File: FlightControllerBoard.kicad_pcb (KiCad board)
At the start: 2 copper layers, 60 x 40 mm, 82 parts, among them J1 Conn_01x02, J10 Conn_01x02, J11 Conn_01x02, J12 Conn_01x03_Male, J13 USB_C_Receptacle_USB2.0, J14 Conn_02x03_Odd_Even, J2 Conn_01x03_Male, J3 Conn_01x03_Male, J4 Conn_01x03_Male, J5 Conn_01x03_Male, J6 Conn_01x03_Male, J7 Conn_01x03_Male, J8 Conn_01x03_Male, J9 Conn_01x03_Male, Q1 BSS138, SW1 SW_Push, SW2 SW_Push, U1 FT230XQ, U2 LMZM23600, U3 ATmega2560-16AU, U4 BNO055, Y1 16MHz, Y2 32.768kHz

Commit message: use submodule for FT230
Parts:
- removed the R8 at (59.0, 71.5)
- removed the R9 at (59.0, 73.5)
- added C5: 4.7µF, Capacitor_SMD:C_0603_1608Metric, F.Cu at (5.52, 0.76)
- moved C4 43.8 mm to (1.51, 0.76), turned to 0 degrees
- renumbered C9 to C10, C10 to C11, C11 to C12, C12 to C13, C13 to C14, C14 to C15, C15 to C16, C16 to C17, C17 to C18, C18 to C19, C19 to C20, C20 to C21, C5 to C6, C6 to C7, C7 to C8, C8 to C9, R12 to R10, R13 to R11, R14 to R12, R15 to R13, R16 to R14, R17 to R15, R18 to R16, R19 to R17, R20 to R18, R21 to R19, R22 to R20, R23 to R21, R24 to R22, R25 to R23, R26 to R24, R10 to R8, R11 to R9
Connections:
- C4 pad 1: VBUS -> /FT230/5VOUT

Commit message: pullups, jumpers
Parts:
- removed the J10 at (258.0, 77.0)
- removed the J11 at (254.0, 77.0)
- added JP1: Jumper_NO_Small, Connector_PinHeader_2.54mm:PinHeader_1x02_P2.54mm_Vertical, F.Cu at (127.8, -48.2)
- added JP2: Jumper_NO_Small, Connector_PinHeader_2.54mm:PinHeader_1x02_P2.54mm_Vertical, F.Cu at (132.5, -48.2)
- added R1: 4.7k, Resistor_SMD:R_0603_1608Metric, F.Cu at (136.8, -49.2)
- added R2: 4.7k, Resistor_SMD:R_0603_1608Metric, F.Cu at (136.8, -46.7)
- renumbered J12 to J10, J13 to J11, J14 to J12, R8 to R10, R9 to R11, R10 to R12, R11 to R13, R12 to R14, R13 to R15, R14 to R16, R15 to R17, R16 to R18, R17 to R19, R18 to R20, R19 to R21, R20 to R22, R21 to R23, R22 to R24, R23 to R25, R24 to R26, R1 to R3, R2 to R4, R3 to R5, R4 to R6, R5 to R7, R6 to R8, R7 to R9

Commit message: layout
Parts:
- removed SW2: SW_Push, Button_Switch_SMD:SW_SPST_PTS810
- added H1: MountingHole, MountingHole:MountingHole_3.2mm_M3, F.Cu at (45.0, 55.0)
- added H2: MountingHole, MountingHole:MountingHole_3.2mm_M3, F.Cu at (5.00, 20.0)
- added H3: MountingHole, MountingHole:MountingHole_3.2mm_M3, F.Cu at (45.0, 20.0)
- added H4: MountingHole, MountingHole:MountingHole_3.2mm_M3, F.Cu at (5.00, 55.0)
- added REF**: ToolboxLogo, Toolbox:ToolboxLogo, F.Cu at (8.25, 47.0)
- J1: footprint XT30:XT30PB-M -> Connector_AMASS:AMASS_XT30UPB-M_1x02_P5.0mm_Vertical
- moved D2 239.7 mm to (18.8, 55.8), turned to 90 degrees
- moved R5 239.3 mm to (18.8, 52.5), turned to 270 degrees
- moved SW1 237.9 mm to (3.25, 13.5), turned to 180 degrees
- moved D1 227.7 mm to (17.0, 55.8), turned to 90 degrees
- moved R4 227.3 mm to (17.0, 52.5), turned to 270 degrees
- moved C19 224.6 mm to (15.5, 39.0), turned to 180 degrees
- moved Y2 221.4 mm to (15.5, 42.0), turned to 90 degrees
- moved C20 219.4 mm to (14.5, 45.8), turned to 270 degrees
- moved U4 218.7 mm to (19.5, 41.0), turned to 90 degrees
- moved C18 215.9 mm to (16.2, 45.8), turned to 270 degrees
- moved R26 213.3 mm to (18.8, 46.8), turned to 180 degrees
- moved C16 211.9 mm to (22.0, 45.0), turned to 0 degrees
- moved C21 211.7 mm to (18.8, 45.0), turned to 180 degrees
- moved R1 135.6 mm to (33.0, 38.0), turned to 180 degrees
- moved R2 132.9 mm to (33.0, 36.2), turned to 180 degrees
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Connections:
- U3 pad 35: (no net) -> Net-(R15-Pad1)
- U3 pad 36: (no net) -> Net-(R16-Pad1)
- U3 pad 37: (no net) -> Net-(R17-Pad1)
- U3 pad 38: (no net) -> Net-(R18-Pad1)
- U3 pad 39: (no net) -> Net-(R19-Pad1)
- U3 pad 40: (no net) -> Net-(R20-Pad1)
- U3 pad 41: (no net) -> Net-(R21-Pad1)
- U3 pad 42: (no net) -> Net-(R22-Pad1)
- U3 pad 53: Net-(R15-Pad1) -> (no net)
- U3 pad 54: Net-(R16-Pad1) -> (no net)
- U3 pad 55: Net-(R17-Pad1) -> (no net)
- U3 pad 56: Net-(R18-Pad1) -> (no net)
- U3 pad 57: Net-(R19-Pad1) -> (no net)
- U3 pad 58: Net-(R20-Pad1) -> (no net)
- U3 pad 59: Net-(R21-Pad1) -> (no net)
- U3 pad 60: Net-(R22-Pad1) -> (no net)
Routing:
- net +3V3: track 24.9 -> 161.8 mm, vias 0 -> 6
- net /ATMega/~RESET~: track 0.00 -> 52.4 mm, vias 0 -> 2
- net +5V: track 74.0 -> 119.0 mm, vias 0 -> 2
- net /FT230/RX: track 1.07 -> 30.5 mm, vias 0 -> 2
- net /ATMega/RX0: track 0.00 -> 25.8 mm, vias 0 -> 2
- net GNDS: track 0.00 -> 16.8 mm, vias 0 -> 2
- net /ATMega/RX1: track 0.00 -> 14.8 mm
- net Net-(R22-Pad1): track 4.96 -> 19.6 mm, vias 0 -> 2
- net Net-(R21-Pad1): track 4.76 -> 18.5 mm, vias 0 -> 2
- net /BNO/INT: track 0.00 -> 13.5 mm, vias 0 -> 2
- net /BNO/RX: track 0.00 -> 12.6 mm
- net Net-(R20-Pad1): track 5.38 -> 17.4 mm, vias 0 -> 2
- net /FT230/5VOUT: track 5.12 -> 17.1 mm, vias 0 -> 1
- net /ATMega/MOSI: track 16.6 -> 28.4 mm
- net /ATMega/SCK: track 15.5 -> 26.5 mm
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- added copper zone on F.Cu, net GNDS
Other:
- board size 60 x 40 mm -> 50 x 60 mm
- net class Default: clearance 0.2 -> 0.15; trace_width 0.25 -> 0.2; via_dia 0.8 -> 0.5; via_drill 0.4 -> 0.25
- rule trace_clearance: 0.2 -> 0.15
- board text added: "1"
- board text added: "2"
- board text added: "3"
- board text added: "3V"
- board text added: "4"
- board text added: "5"
- board text added: "5V"
- board text added: "5V In"
- board text added: "6"
- board text added: "7"
- board text added: "8"
- board text added: "GND"
- board text added: "ICSP"
- board text added: "REMOVE BEFORE FLIGHT"
- board text added: "RX"
- board text added: "SB"
- board text added: "TX"

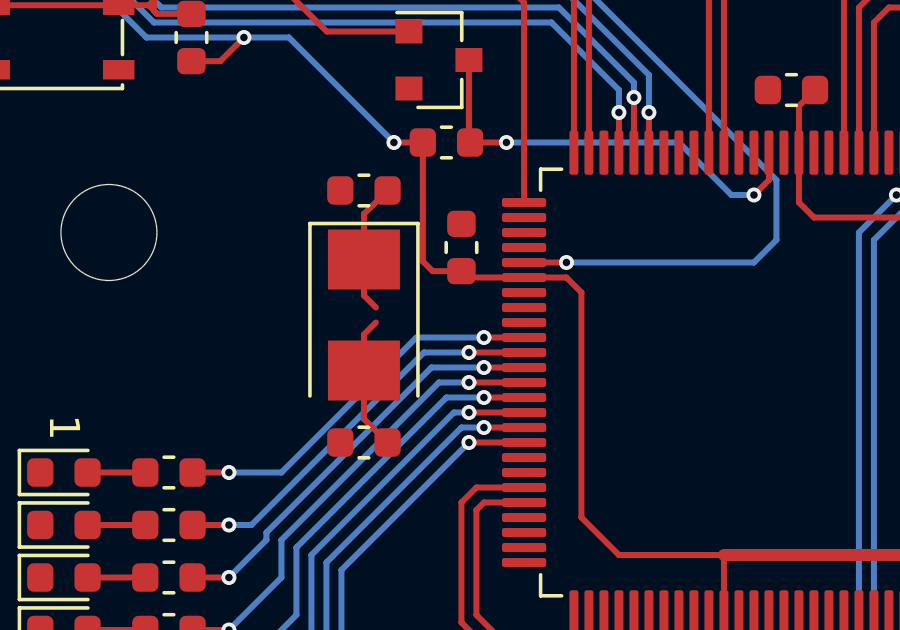
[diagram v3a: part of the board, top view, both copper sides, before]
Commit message: fix Y1 connection
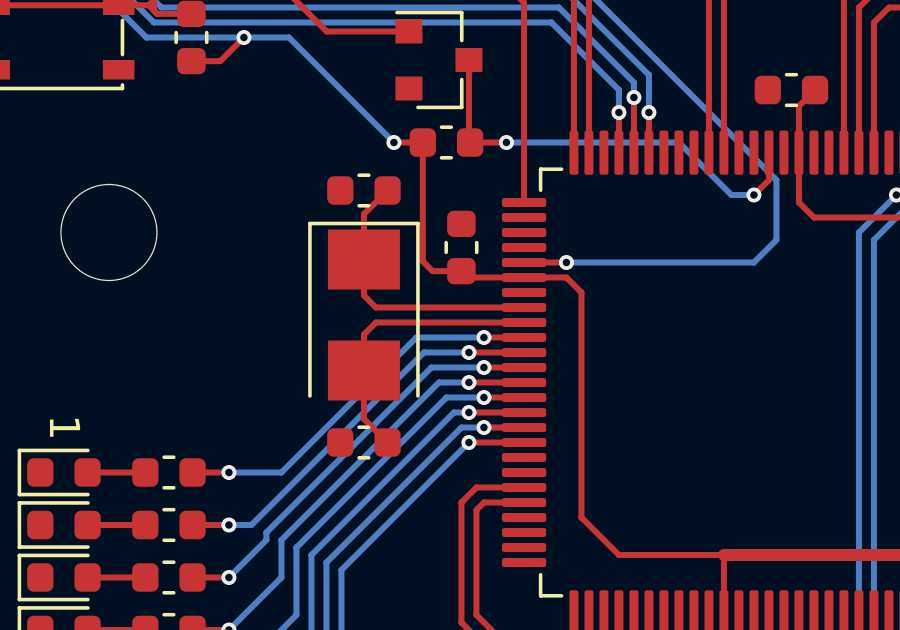
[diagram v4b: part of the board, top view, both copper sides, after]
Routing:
- net Net-(C9-Pad1): track 4.49 -> 9.43 mm
- net Net-(C10-Pad1): track 4.39 -> 9.33 mm
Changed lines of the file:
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@@
     (thickness 1.6)
     (drawings 35)
-    (tracks 485)
+    (tracks 487)
     (zones 0)
     (modules 87)
@@
   (segment (start 13.5 23.4) (end 13.5 24.6) (width 0.2) (layer F.Cu) (net 44) (status 20))
   (segment (start 13.9 23) (end 13.5 23.4) (width 0.2) (layer F.Cu) (net 44))
+  (segment (start 13.9 23) (end 18.8375 23) (width 0.2) (layer F.Cu) (net 44))
   (segment (start 15.5 39.7875) (end 16.2875 39) (width 0.2) (layer F.Cu) (net 45) (status 20))
   (segment (start 15.5 40.75) (end 15.5 39.7875) (width 0.2) (layer F.Cu) (net 45) (status 10))
@@
   (segment (start 13.5 22.1) (end 13.5 20.9) (width 0.2) (layer F.Cu) (net 51) (status 20))
   (segment (start 13.9 22.5) (end 13.5 22.1) (width 0.2) (layer F.Cu) (net 51))
+  (segment (start 13.9 22.5) (end 18.8375 22.5) (width 0.2) (layer F.Cu) (net 51))
   (segment (start 22.7125 41.75) (end 22.75 41.7125) (width 0.2) (layer F.Cu) (net 52) (status 30))
   (segment (start 21.1625 41.75) (end 22.7125 41.75) (width 0.2) (layer F.Cu) (net 52) (status 30))

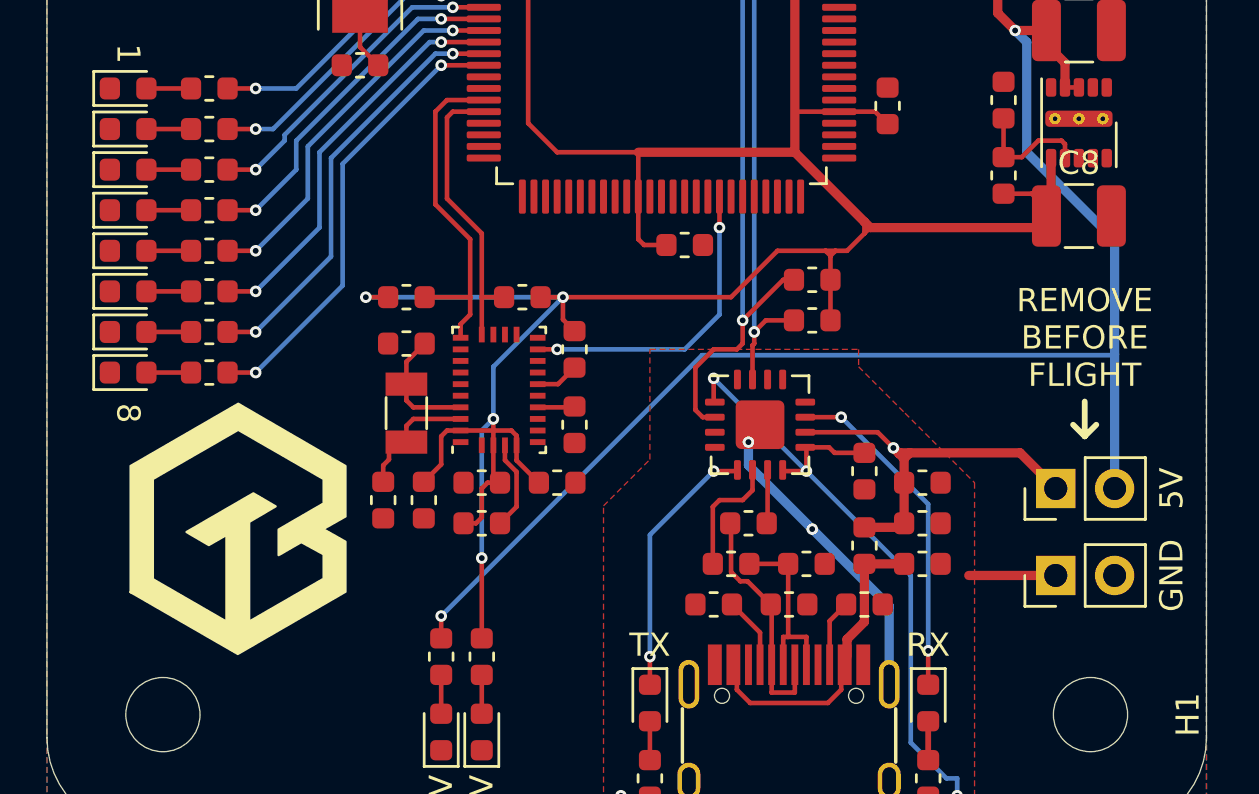
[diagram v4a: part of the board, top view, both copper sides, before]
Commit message: small layout fixes
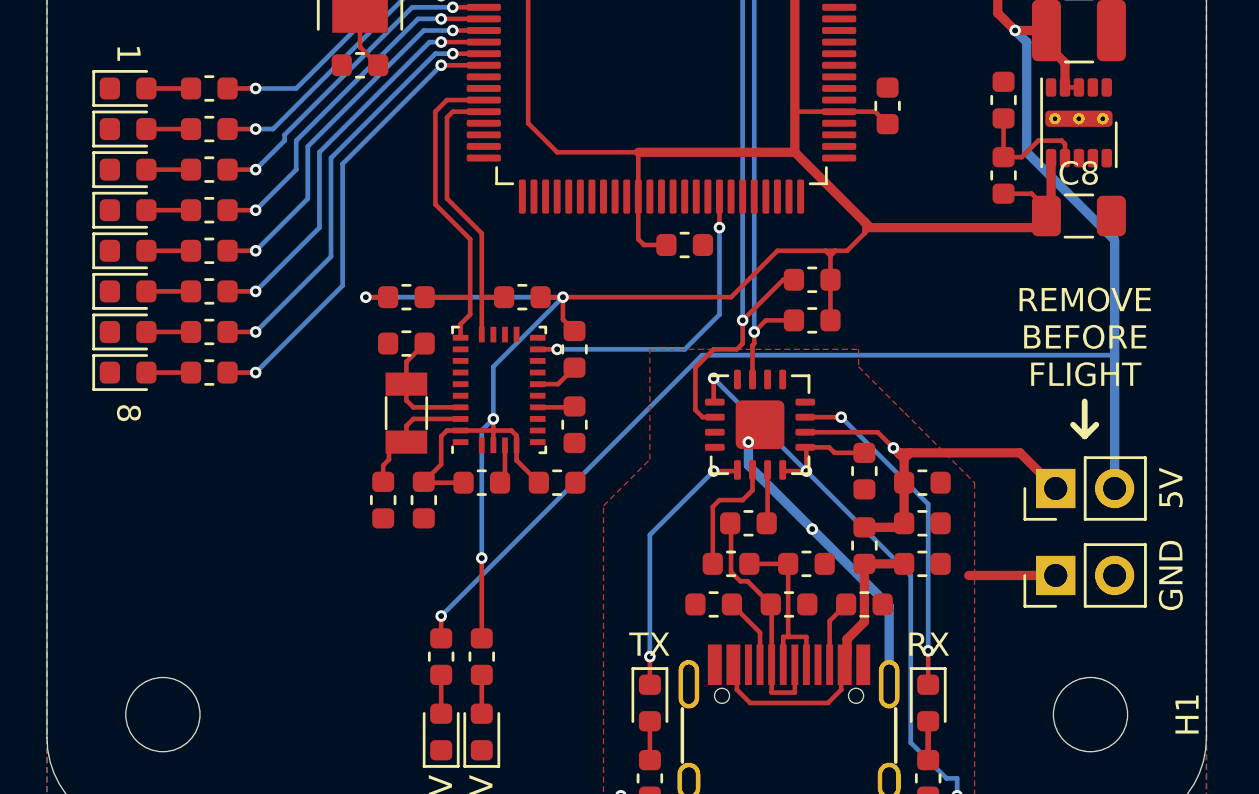
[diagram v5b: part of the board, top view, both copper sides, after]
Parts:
- removed C21: 6.8nF, Capacitor_SMD:C_0603_1608Metric
- removed REF**: ToolboxLogo, Toolbox:ToolboxLogo
- C18: value 120nF -> 100nF
- C19, C20: value 12.5pF -> 9pF
- C8: value 33µF -> 22µF; footprint Capacitor_SMD:C_1210_3225Metric -> Capacitor_SMD:C_1206_3216Metric
- moved R26 1.75 mm to (18.8, 45.0)
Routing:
- net +3V3: track 161.8 -> 158.8 mm
- net Net-(R26-Pad1): track 3.86 -> 1.70 mm

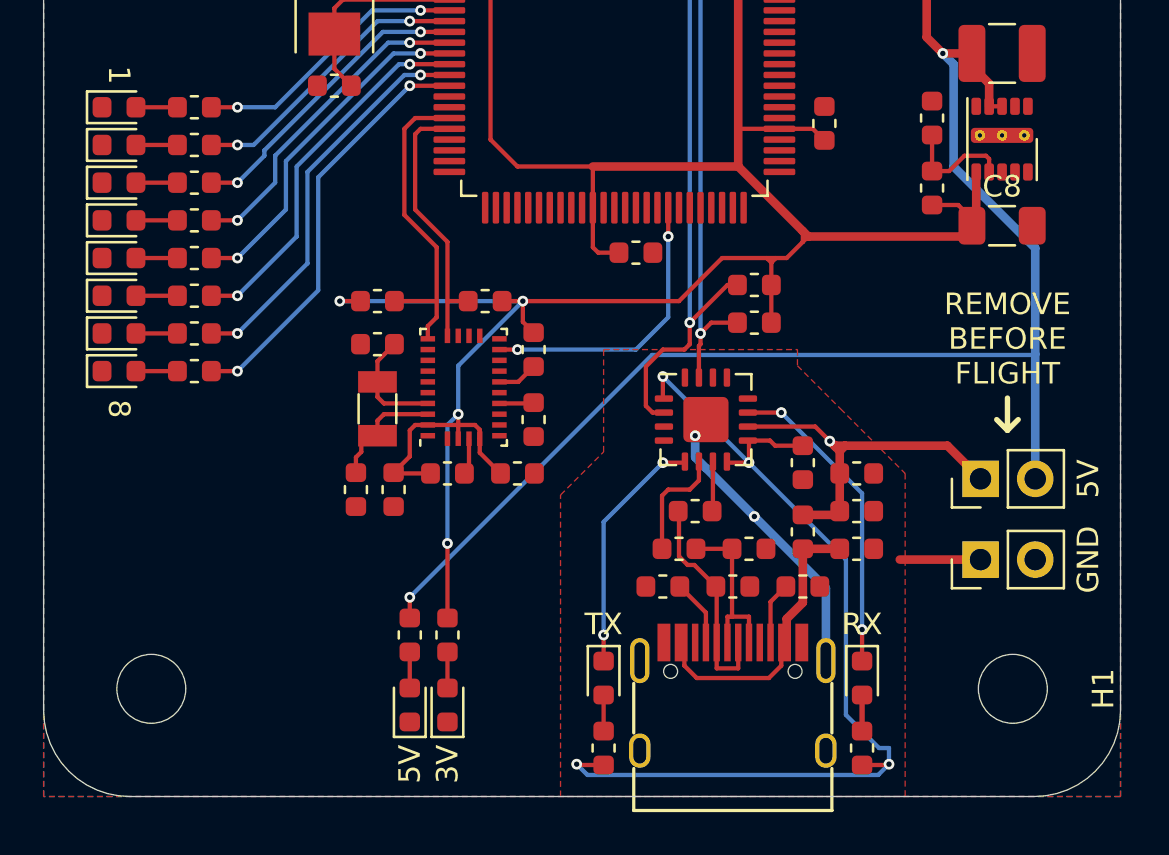
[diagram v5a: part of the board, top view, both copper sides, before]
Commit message: silkscreen logos
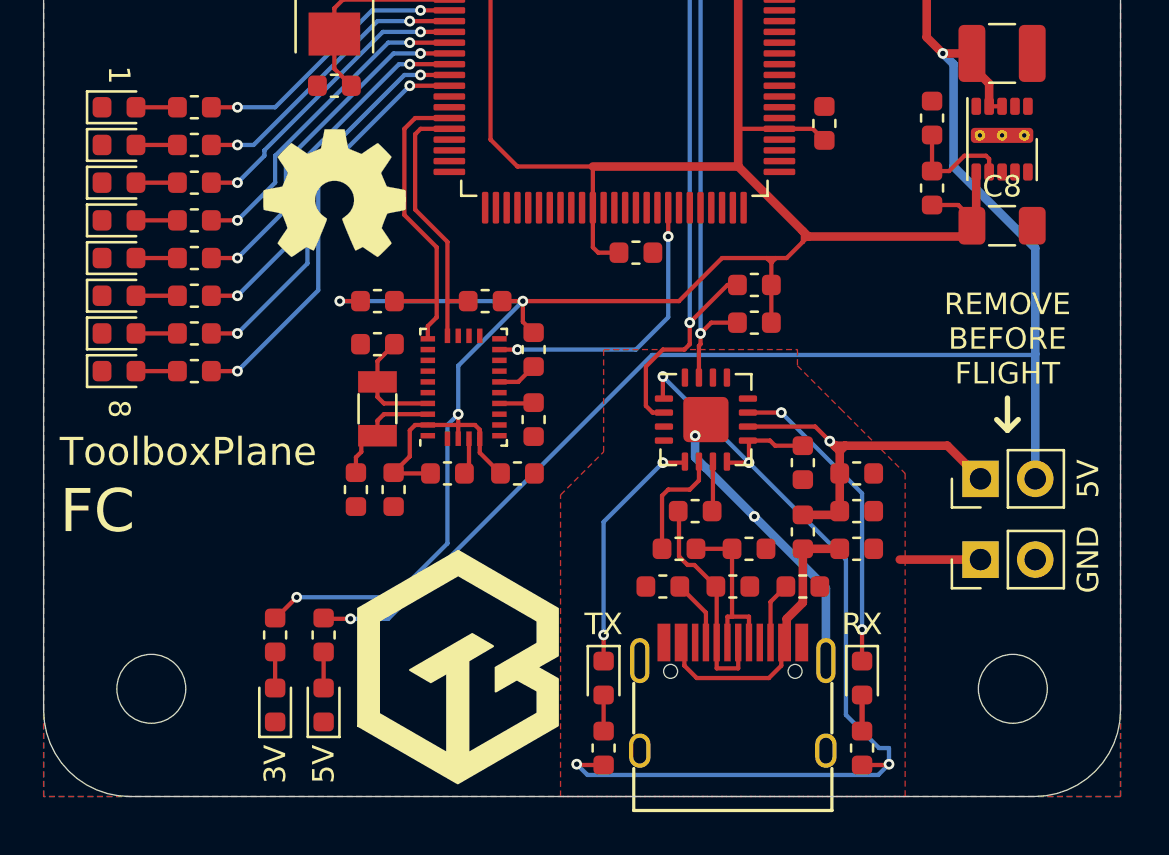
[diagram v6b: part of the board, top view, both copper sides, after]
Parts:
- added REF**: OSHW-Symbol_6.7x6mm_SilkScreen, Symbol:OSHW-Symbol_6.7x6mm_SilkScreen, F.Cu at (13.5, 32.0)
- added REF**: ToolboxLogo_Large, Toolbox:ToolboxLogo_Large, B.Cu at (25.0, 37.5)
- added REF**: ToolboxLogo, Toolbox:ToolboxLogo, F.Cu at (19.2, 54.0)
- moved D2 8.00 mm to (10.8, 55.8)
- moved R5 8.00 mm to (10.8, 52.5)
- moved D1 4.00 mm to (13.0, 55.8)
- moved R4 4.00 mm to (13.0, 52.5)
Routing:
- net +3V3: track 158.8 -> 164.7 mm
- net +5V: track 119.0 -> 122.5 mm
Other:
- board text added: "FC"
- board text added: "ToolboxPlane"
